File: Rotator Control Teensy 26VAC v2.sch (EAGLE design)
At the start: 65 parts, among them K1 G5LE, K2 G5LE, K3 G5LE, Q1 BSS123, Q2 BSS123, Q3 BSS123, U2 MAX6959BAEE+, X1 Rotor, X2 26VAC

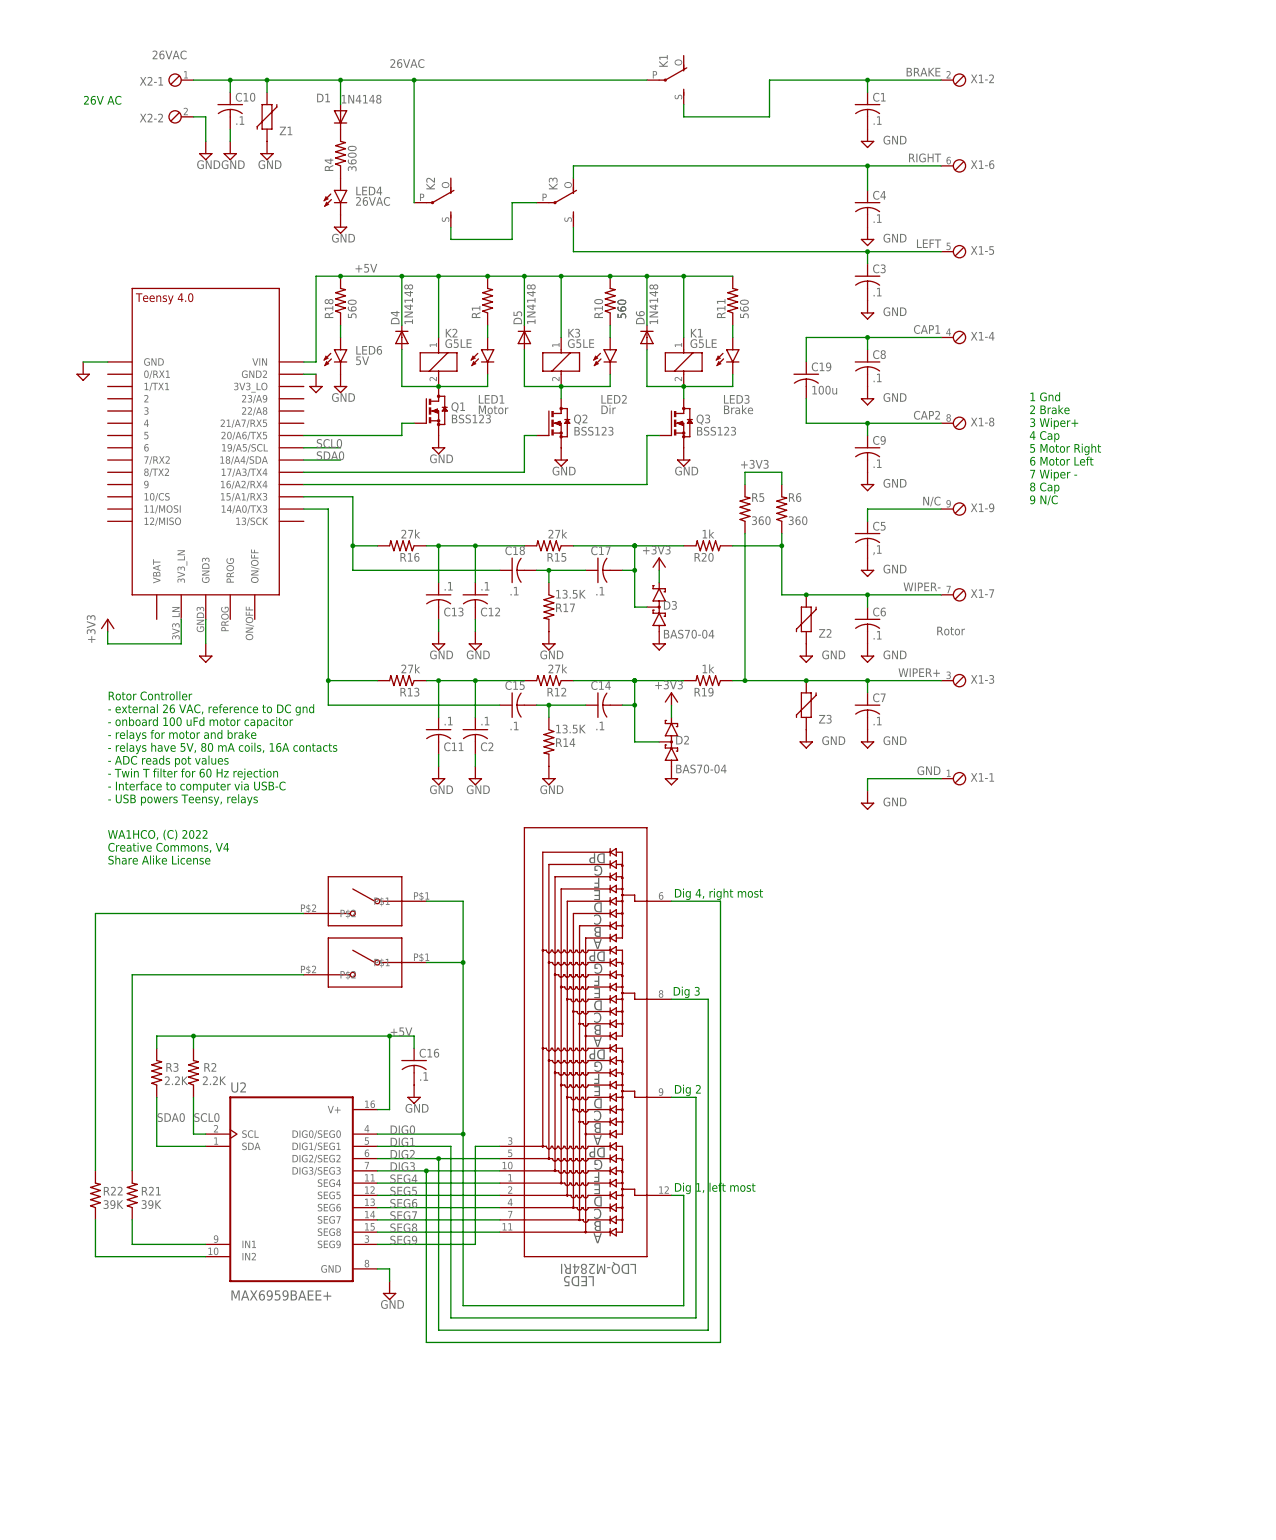
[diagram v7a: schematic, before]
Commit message: Convert to MAX7221 LED driver Connect MAX7221 to SPI port Convert buttons to direct read with internal pullups
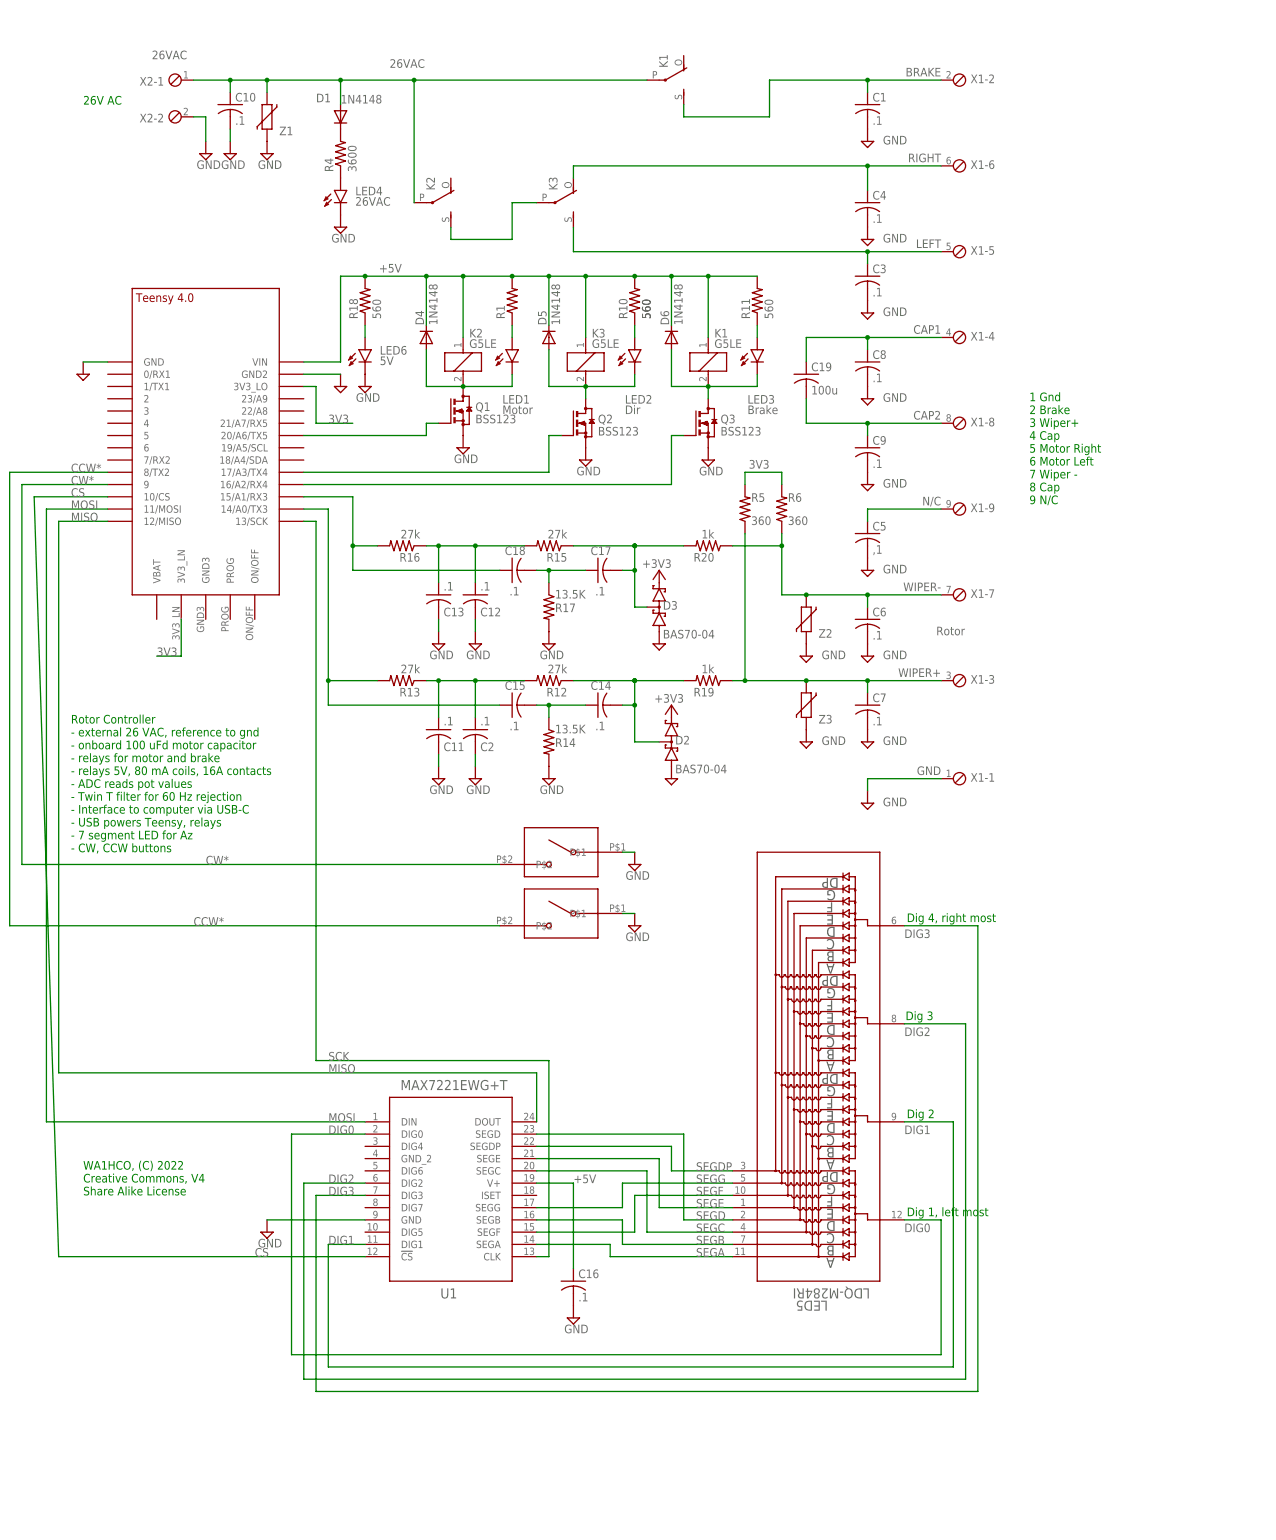
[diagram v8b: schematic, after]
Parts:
- removed R2, R3: 2.2K, rcl:R-US_R0805
- removed R21, R22: 39K, rcl:R-US_R0805
- removed U$2, U$3: SWITCH_AEXIT_6X6X9.5, my-library:SWITCH_AEXIT_6X6X9.5
- removed U2: MAX6959BAEE+, MAX6959BAEE_:MAX6959BAEE+
- added CCW, CW: SWITCH_AEXIT_6X6X9.5, my-library:SWITCH_AEXIT_6X6X9.5
- added U1: MAX7221EWG+T, MAX7219:MAX7221EWG+T
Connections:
- removed net +3V3: D2.C2, D3.C2, R5.2, R6.2, U$1.3V3_LN
- removed net N$15: R21.1, U2.IN1
- removed net N$16: R22.1, U2.IN2
- removed net N$19: R21.2, U$3.P$2
- removed net N$20: R22.2, U$2.P$2
- removed net SCL0: R2.1, U$1.19/A5/SCL, U2.SCL
- removed net SDA0: R3.1, U$1.18/A4/SDA, U2.SDA
- removed net SEG4: LED5.1, U2.SEG4
- removed net SEG5: LED5.2, U2.SEG5
- removed net SEG6: LED5.4, U2.SEG6
- removed net SEG7: LED5.7, U2.SEG7
- removed net SEG8: LED5.11, U2.SEG8
- removed net SEG9: LED5.3, U2.SEG9
- new net 3V3: D2.C2, D3.C2, R5.2, R6.2, U$1.3V3_LN, U$1.3V3_LO
- new net CCW*: CCW.P$2, U$1.8/TX2
- new net CS: U$1.10/CS, U1.!CS
- new net CW*: CW.P$2, U$1.9
- new net MISO: U$1.12/MISO, U1.DOUT
- new net MOSI: U$1.11/MOSI, U1.DIN
- new net SCK: U$1.13/SCK, U1.CLK
- new net SEGA: LED5.11, U1.SEGA
- new net SEGB: LED5.7, U1.SEGB
- new net SEGC: LED5.4, U1.SEGC
- new net SEGD: LED5.2, U1.SEGD
- new net SEGDP: LED5.3, U1.SEGDP
- new net SEGE: LED5.1, U1.SEGE
- new net SEGF: LED5.10, U1.SEGF
- new net SEGG: LED5.5, U1.SEGG
- net +5V: now also U1.V+; no longer R2.2, R3.2, U2.V+
- net DIG0: now also U1.DIG0; no longer U$2.P$1, U$3.P$1, U2.DIG0/SEG0
- net DIG1: now also U1.DIG1; no longer U2.DIG1/SEG1
- net DIG2: now also U1.DIG2; no longer LED5.5, U2.DIG2/SEG2
- net DIG3: now also U1.DIG3; no longer LED5.10, U2.DIG3/SEG3
- net GND: now also CCW.P$1, CW.P$1, U1.GND; no longer U$1.GND3, U2.GND
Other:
- note added: "Rotor Controller - external 26 VAC, reference to gnd - onboard 100 uFd motor capacitor - relays for motor and brake - relays 5V, 80 mA coils, 16A contacts - ADC reads pot values - Twin T filter for 60 Hz rejection - Interface to computer via USB-C - USB powers Teensy, relays - 7 segment LED for Az - CW, CCW buttons"
- note removed: "Rotor Controller - external 26 VAC, reference to DC gnd - onboard 100 uFd motor capacitor - relays for motor and brake - relays have 5V, 80 mA coils, 16A contacts - ADC reads pot values - Twin T filter for 60 Hz rejection - Interface to computer via USB-C - USB powers Teensy, relays"
- moved on the sheet: C16, D4, D5, D6, K1, K2, K3, LED1, LED2, LED3, LED5, LED6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
